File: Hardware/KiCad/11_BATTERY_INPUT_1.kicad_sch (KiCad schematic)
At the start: 0 parts

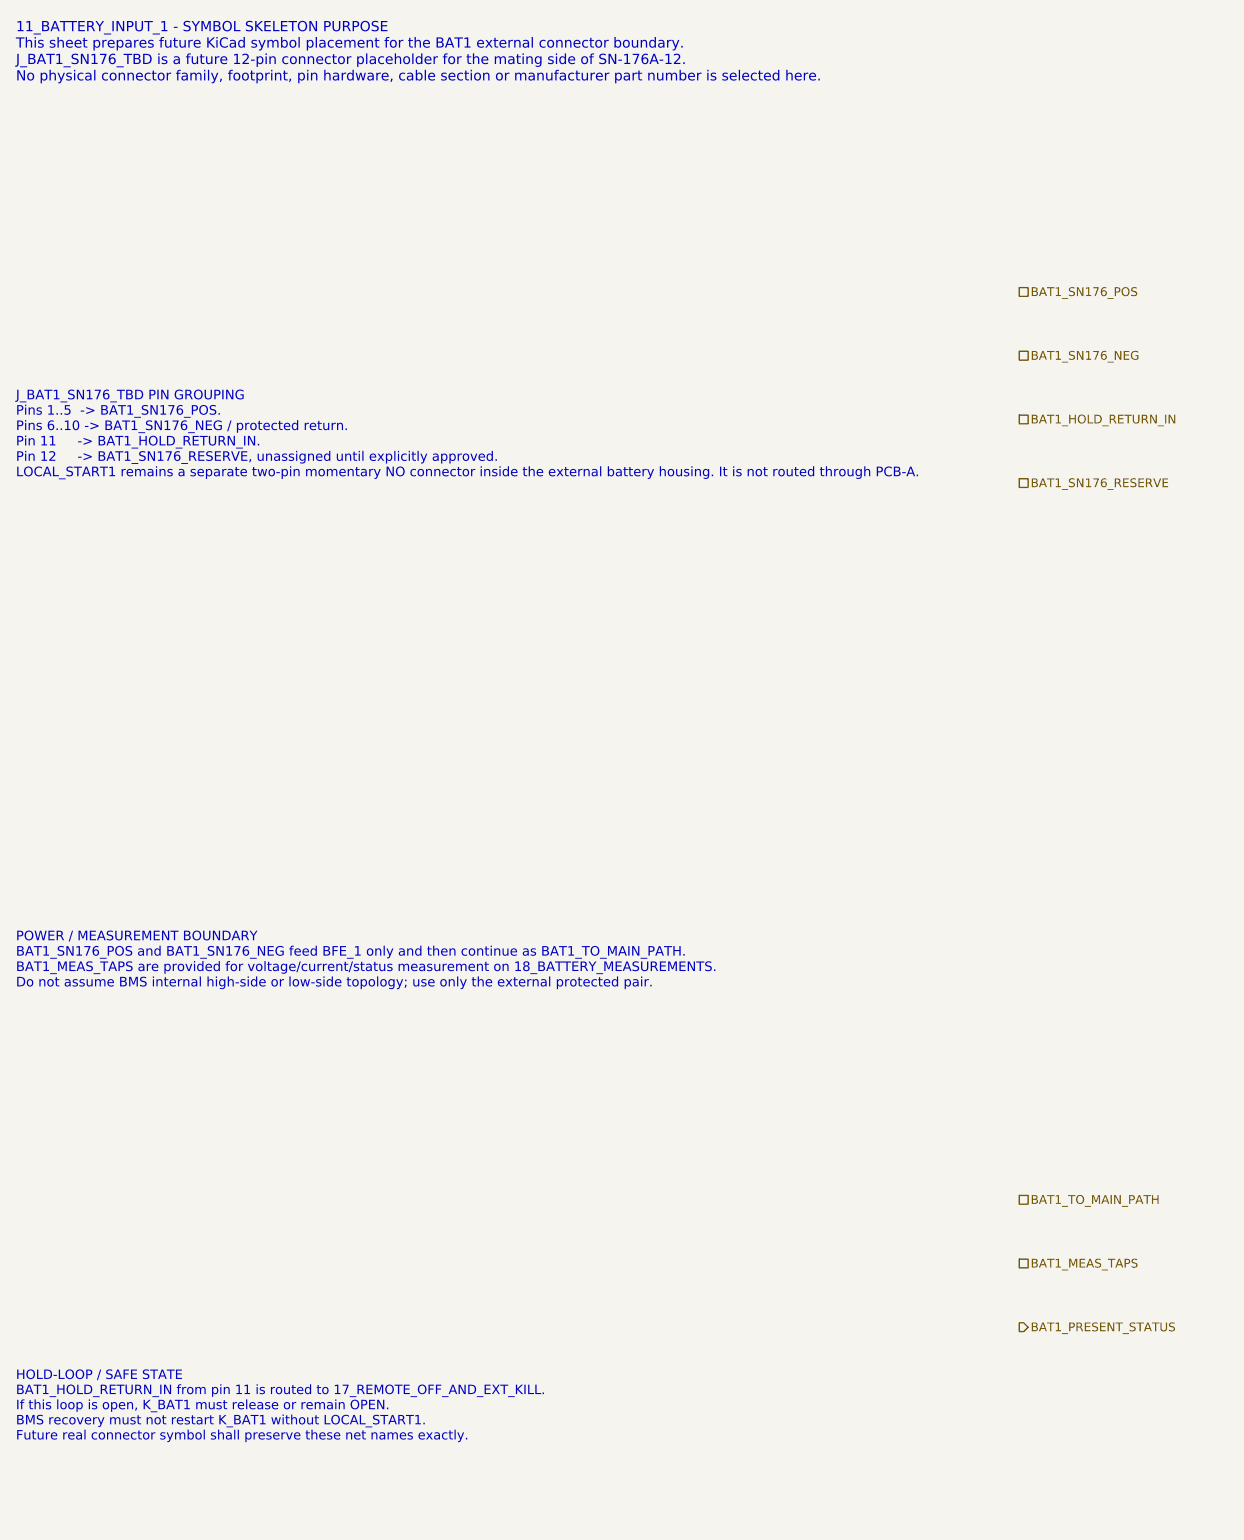
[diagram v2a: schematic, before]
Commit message: hardware: check PCB-A BFE interface consistency
Merge PR #23 after confirming PCB-A BFE interface consistency passes with controlled placeholders.
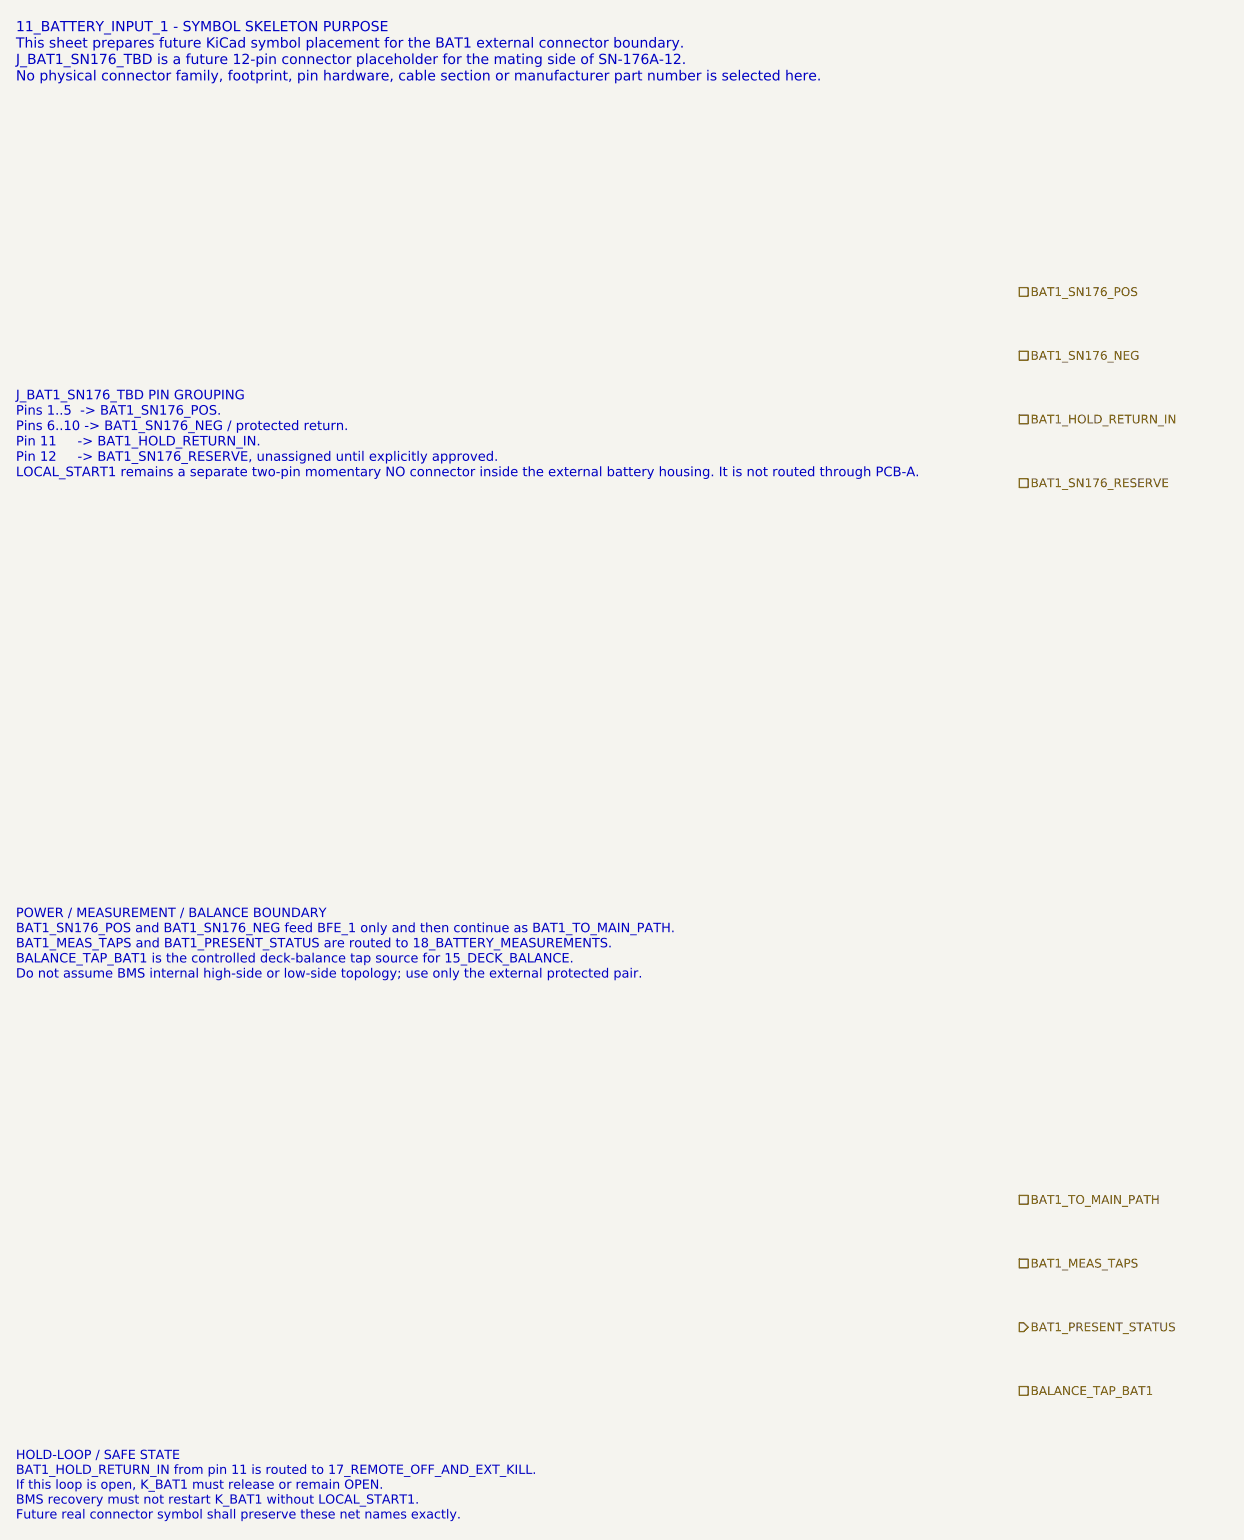
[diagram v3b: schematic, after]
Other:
- note added: "POWER / MEASUREMENT / BALANCE BOUNDARY BAT1_SN176_POS and BAT1_SN176_NEG feed BFE_1 only and then continue as BAT1_TO_MAIN_PATH. BAT1_MEAS_TAPS and BAT1_PRESENT_STATUS are routed to 18_BATTERY_MEASUREMENTS. BALANCE_TAP_BAT1 is the controlled deck-balance tap source for 15_DECK_BALANCE. Do not assume BMS internal high-side or low-side topology; use only the external protected pair."
- note removed: "POWER / MEASUREMENT BOUNDARY BAT1_SN176_POS and BAT1_SN176_NEG feed BFE_1 only and then continue as BAT1_TO_MAIN_PATH. BAT1_MEAS_TAPS are provided for voltage/current/status measurement on 18_BATTERY_MEASUREMENTS. Do not assume BMS internal high-side or low-side topology; use only the external protected pair."
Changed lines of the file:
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@@
 		(title "11_BATTERY_INPUT_1 - BFE input from AKB_1")
 		(date "2026-07-15")
-		(rev "C0")
+		(rev "C1")
 		(company "Gonoboben/plataVM")
-		(comment 1 "Symbol skeleton: BAT1 SN-176A-12 boundary and future connector placement zones")
+		(comment 1 "Interface consistency: BAT1 connector boundary, balance tap and status")
 		(comment 2 "Text-only placeholders; no connector family, footprint, fuse, sensor or contactor selected")
 	)
@@
 		(uuid "bfe-symbol-00000011-0000-4000-8000-000000000102")
 	)
-	(text "POWER / MEASUREMENT BOUNDARY\nBAT1_SN176_POS and BAT1_SN176_NEG feed BFE_1 only and then continue as BAT1_TO_MAIN_PATH.\nBAT1_MEAS_TAPS are provided for voltage/current/status measurement on 18_BATTERY_MEASUREMENTS.\nDo not assume BMS internal high-side or low-side topology; use only the external protected pair."
+	(text "POWER / MEASUREMENT / BALANCE BOUNDARY\nBAT1_SN176_POS and BAT1_SN176_NEG feed BFE_1 only and then continue as BAT1_TO_MAIN_PATH.\nBAT1_MEAS_TAPS and BAT1_PRESENT_STATUS are routed to 18_BATTERY_MEASUREMENTS.\nBALANCE_TAP_BAT1 is the controlled deck-balance tap source for 15_DECK_BALANCE.\nDo not assume BMS internal high-side or low-side topology; use only the external protected pair."
 		(exclude_from_sim no)
-		(at 12 128 0)
-		(effects (font (size 1.20 1.20)) (justify left))
+		(at 12 126 0)
+		(effects (font (size 1.18 1.18)) (justify left))
 		(uuid "bfe-symbol-00000011-0000-4000-8000-000000000103")
 	)
 	(text "HOLD-LOOP / SAFE STATE\nBAT1_HOLD_RETURN_IN from pin 11 is routed to 17_REMOTE_OFF_AND_EXT_KILL.\nIf this loop is open, K_BAT1 must release or remain OPEN.\nBMS recovery must not restart K_BAT1 without LOCAL_START1.\nFuture real connector symbol shall preserve these net names exactly."
 		(exclude_from_sim no)
-		(at 12 184 0)
-		(effects (font (size 1.18 1.18)) (justify left))
+		(at 12 194 0)
+		(effects (font (size 1.16 1.16)) (justify left))
 		(uuid "bfe-symbol-00000011-0000-4000-8000-000000000104")
 	)
@@
 	(hierarchical_label "BAT1_MEAS_TAPS" (shape passive) (exclude_from_sim no) (at 138 166 0) (effects (font (size 1.1 1.1)) (justify left)) (uuid "bfe-symbol-00000011-0000-4000-8000-000000000206"))
 	(hierarchical_label "BAT1_PRESENT_STATUS" (shape output) (exclude_from_sim no) (at 138 174 0) (effects (font (size 1.1 1.1)) (justify left)) (uuid "bfe-symbol-00000011-0000-4000-8000-000000000207"))
+	(hierarchical_label "BALANCE_TAP_BAT1" (shape passive) (exclude_from_sim no) (at 138 182 0) (effects (font (size 1.1 1.1)) (justify left)) (uuid "bfe-symbol-00000011-0000-4000-8000-000000000208"))
 )
